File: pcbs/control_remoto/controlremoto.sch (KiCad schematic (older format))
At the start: 37 parts, among them P1 CONN_BATT, P10 CONN_BTN04, P11 CONN_BTN09, P12 CONN_MIC, P13 DIPSWITCH, P2 CONN_BTN00, P3 CONN_BTN05, P4 CONN_BTN01, P5 CONN_BTN06, P6 CONN_BTN02, P7 CONN_BTN07, P8 CONN_BTN03, P9 CONN_BTN08, SW1 ON/OFF, U1 MMA7455L_DIP8, U2 PTN4050, U3 MBED, U4 TL082, U5 ZIGBIT_DUAL_DIP

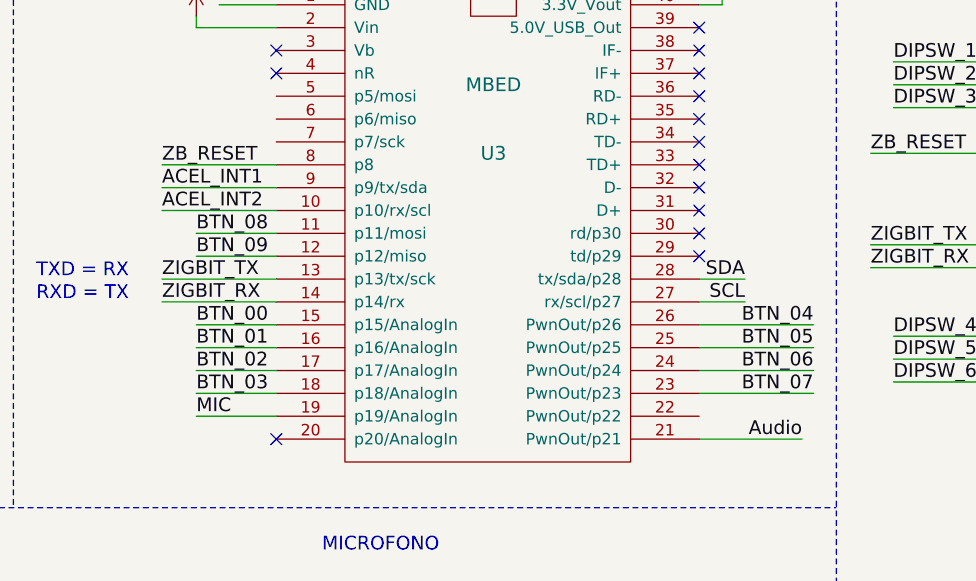
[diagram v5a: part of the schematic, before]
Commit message: primera version del control, falta verificar footprint
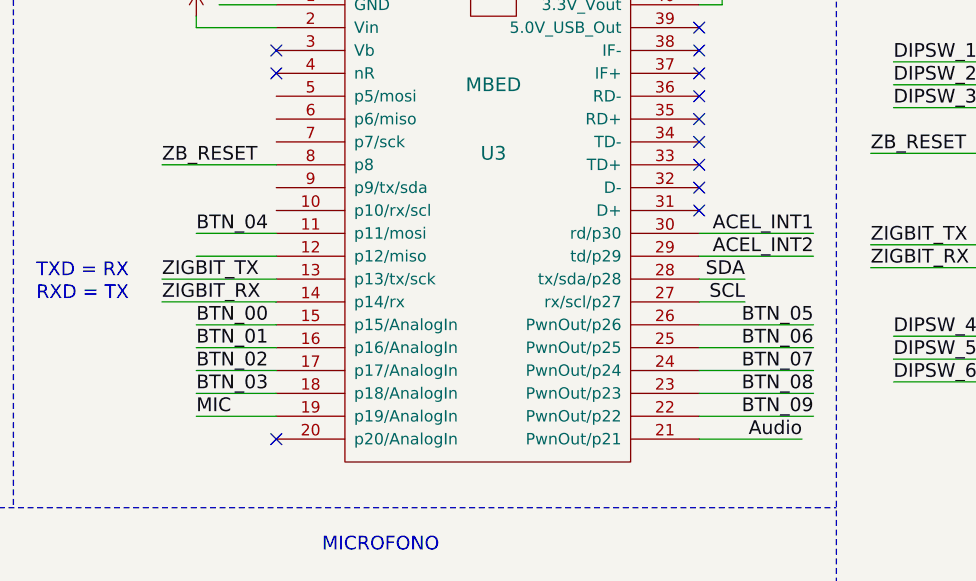
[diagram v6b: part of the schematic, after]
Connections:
- net ACEL_INT1: now also U3.30 (rd/p30); no longer U3.9 (p9/tx/sda)
- net ACEL_INT2: now also U3.29 (td/p29); no longer U3.10 (p10/rx/scl)
- net BTN_04: now also U3.11 (p11/mosi); no longer U3.26 (PwnOut/p26)
- net BTN_05: now also U3.26 (PwnOut/p26); no longer U3.25 (PwnOut/p25)
- net BTN_06: now also U3.25 (PwnOut/p25); no longer U3.24 (PwnOut/p24)
- net BTN_07: now also U3.24 (PwnOut/p24); no longer U3.23 (PwnOut/p23)
- net BTN_08: now also U3.23 (PwnOut/p23); no longer U3.11 (p11/mosi)
- net BTN_09: now also U3.22 (PwnOut/p22); no longer U3.12 (p12/miso)
- no-connect marks 40 -> 38
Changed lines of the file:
@@
 LIBS:zigbit_dual
 LIBS:lm386_mod
+LIBS:controlremoto-cache
 EELAYER 25 0
 EELAYER END
@@
 NoConn ~ 7400 1800
 NoConn ~ 7400 1900
-NoConn ~ 7400 2000
-NoConn ~ 7400 2100
 NoConn ~ 5550 2900
 NoConn ~ 5550 1300
@@
 Text Label 1000 3950 0    60   ~ 0
 GND
-Text Label 5050 1900 0    60   ~ 0
+Text Label 7900 2100 2    60   ~ 0
 ACEL_INT2
-Text Label 5050 1800 0    60   ~ 0
+Text Label 7900 2000 2    60   ~ 0
 ACEL_INT1
 Text Label 5050 2200 0    60   ~ 0
@@
 Text Label 5200 2700 0    60   ~ 0
 BTN_03
+Text Label 5200 2000 0    60   ~ 0
+BTN_04
 Text Label 7900 2400 2    60   ~ 0
-BTN_04
+BTN_05
 Text Label 7900 2500 2    60   ~ 0
-BTN_05
+BTN_06
 Text Label 7900 2600 2    60   ~ 0
-BTN_06
+BTN_07
 Text Label 7900 2700 2    60   ~ 0
-BTN_07
-Text Label 5200 2000 0    60   ~ 0
 BTN_08
-Text Label 5200 2100 0    60   ~ 0
+Text Label 7900 2800 2    60   ~ 0
 BTN_09
 Text Notes 2100 800  0    60   ~ 0
@@
 	1000 3950 1250 3950
 Wire Wire Line
-	5050 1800 5550 1800
-Wire Wire Line
 	2450 3950 3350 3950
 Wire Wire Line
@@
 Wire Wire Line
 	2450 3800 3350 3800
-Wire Wire Line
-	5050 1900 5550 1900
 Wire Wire Line
 	10550 1750 10750 1750
@@
 	0    -1   -1   0
 $EndComp
+Wire Wire Line
+	7900 2800 7400 2800
+Wire Wire Line
+	7900 2100 7400 2100
+Wire Wire Line
+	7900 2000 7400 2000
 $EndSCHEMATC

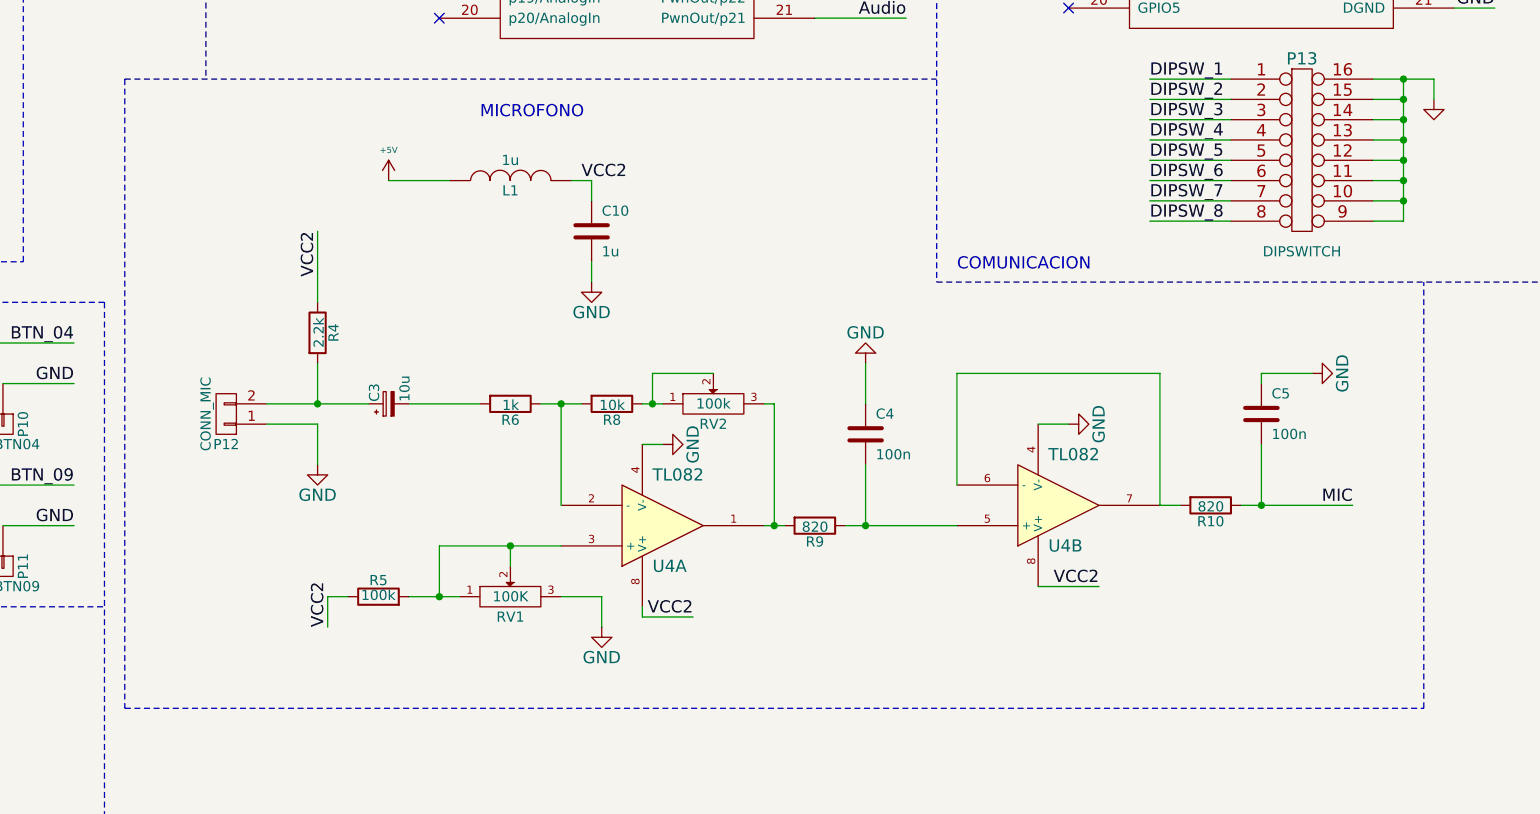
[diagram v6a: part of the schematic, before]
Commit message: actualizo las 3 placas, revisar y mandar a fabricar
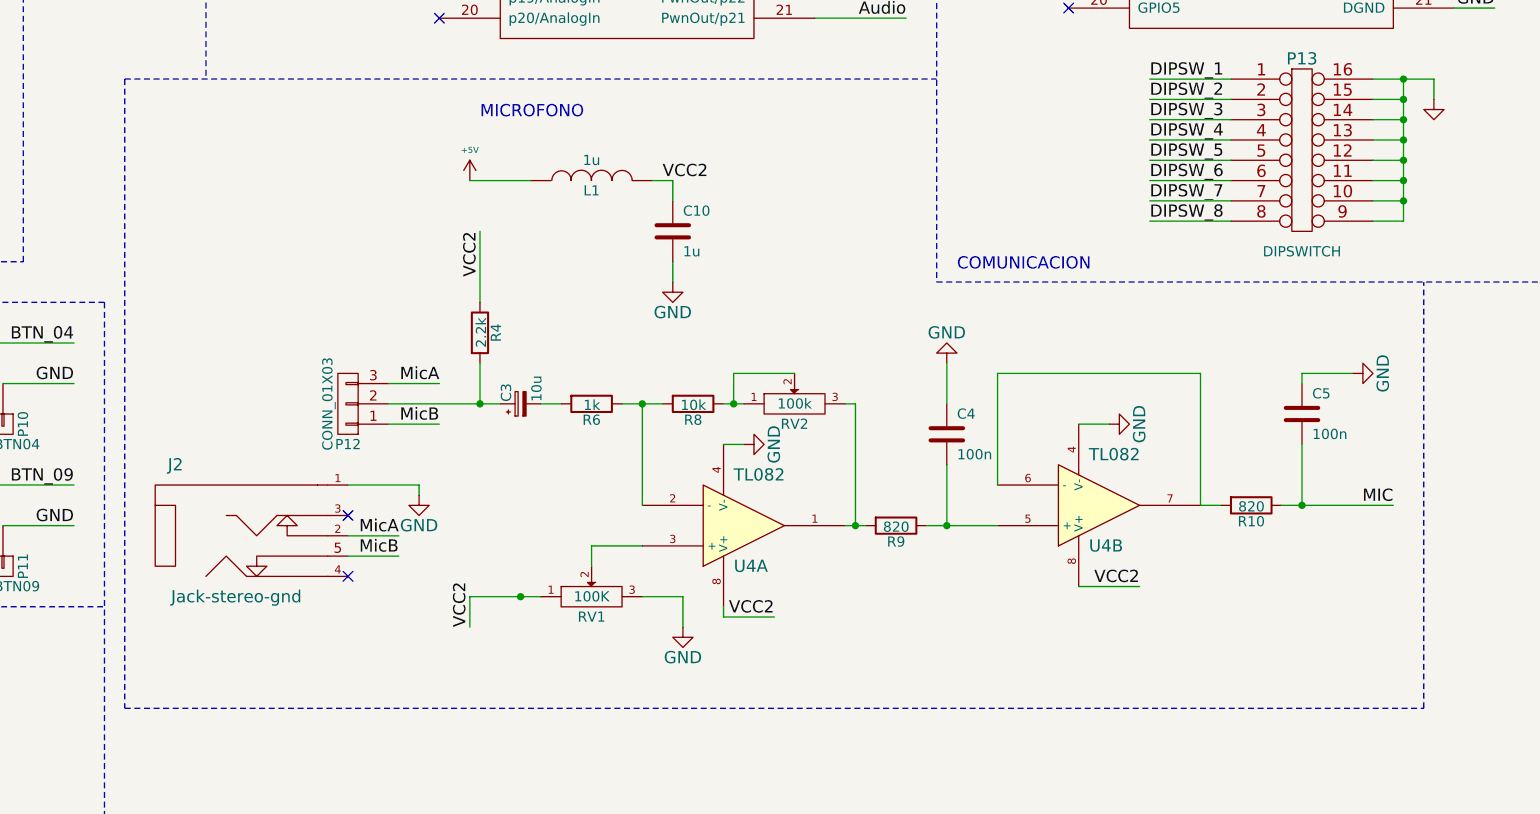
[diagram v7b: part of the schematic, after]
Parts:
- removed P12: CONN_MIC, Connect:PINHEAD1-2, symbol CONN_01X02
- removed R5: 100k, Resistors_ThroughHole:Resistor_Horizontal_RM10mm, symbol R
- added J2: Jack-stereo-gnd, Popurri_CDR:audio-jack-stereo, symbol Jack-stereo-gnd
- added P12: CONN_01X03, Socket_Strips:Socket_Strip_Straight_1x03, symbol CONN_01X03
- C10: footprint Capacitors_ThroughHole:C_Disc_D3_P2.5 -> Capacitors_ThroughHole:C_Rect_L18_W5_P15
- C4, C5: footprint Capacitors_ThroughHole:C_Disc_D3_P2.5 -> Capacitors_ThroughHole:C_Rect_L7_W2_P5
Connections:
- net GND: now also J2.1
- net VCC2: now also RV1.1
- net at C3.1, R4.2: now also P12.2 (P2)
- net at RV1.2, U4.3 (+): no longer RV1.1
- new net MicA: J2.2, P12.3 (P3)
- new net MicB: J2.5, P12.1 (P1)
- no-connect marks 38 -> 40
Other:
- moved on the sheet: C10, C3, C4, C5, L1, R10, R4, R6, R8, R9, RV1, RV2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

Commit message: cambios hechos en las placas
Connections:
- net BTN_00: now also U3.18 (p18/AnalogIn); no longer U3.15 (p15/AnalogIn)
- net BTN_01: now also U3.17 (p17/AnalogIn); no longer U3.16 (p16/AnalogIn)
- net BTN_02: now also U3.16 (p16/AnalogIn); no longer U3.17 (p17/AnalogIn)
- net BTN_03: now also U3.15 (p15/AnalogIn); no longer U3.18 (p18/AnalogIn)
- net BTN_05: now also U3.22 (PwnOut/p22); no longer U3.26 (PwnOut/p26)
- net BTN_06: now also U3.23 (PwnOut/p23); no longer U3.25 (PwnOut/p25)
- net BTN_08: now also U3.25 (PwnOut/p25); no longer U3.23 (PwnOut/p23)
- net BTN_09: now also U3.26 (PwnOut/p26); no longer U3.22 (PwnOut/p22)
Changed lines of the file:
@@
 Text Notes 1950 4300 0    60   ~ 0
 BOTONES
+Text Label 5200 2700 0    60   ~ 0
+BTN_00
+Text Label 5200 2600 0    60   ~ 0
+BTN_01
+Text Label 5200 2500 0    60   ~ 0
+BTN_02
 Text Label 5200 2400 0    60   ~ 0
-BTN_00
-Text Label 5200 2500 0    60   ~ 0
-BTN_01
-Text Label 5200 2600 0    60   ~ 0
-BTN_02
-Text Label 5200 2700 0    60   ~ 0
 BTN_03
 Text Label 5200 2000 0    60   ~ 0
 BTN_04
-Text Label 7900 2400 2    60   ~ 0
+Text Label 7900 2800 2    60   ~ 0
 BTN_05
-Text Label 7900 2500 2    60   ~ 0
+Text Label 7900 2700 2    60   ~ 0
 BTN_06
 Text Label 7900 2600 2    60   ~ 0
 BTN_07
-Text Label 7900 2700 2    60   ~ 0
+Text Label 7900 2500 2    60   ~ 0
 BTN_08
-Text Label 7900 2800 2    60   ~ 0
+Text Label 7900 2400 2    60   ~ 0
 BTN_09
 Text Notes 2100 800  0    60   ~ 0
